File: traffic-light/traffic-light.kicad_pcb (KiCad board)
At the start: 2 copper layers, 11 parts, among them J1 Conn_01x04_Male

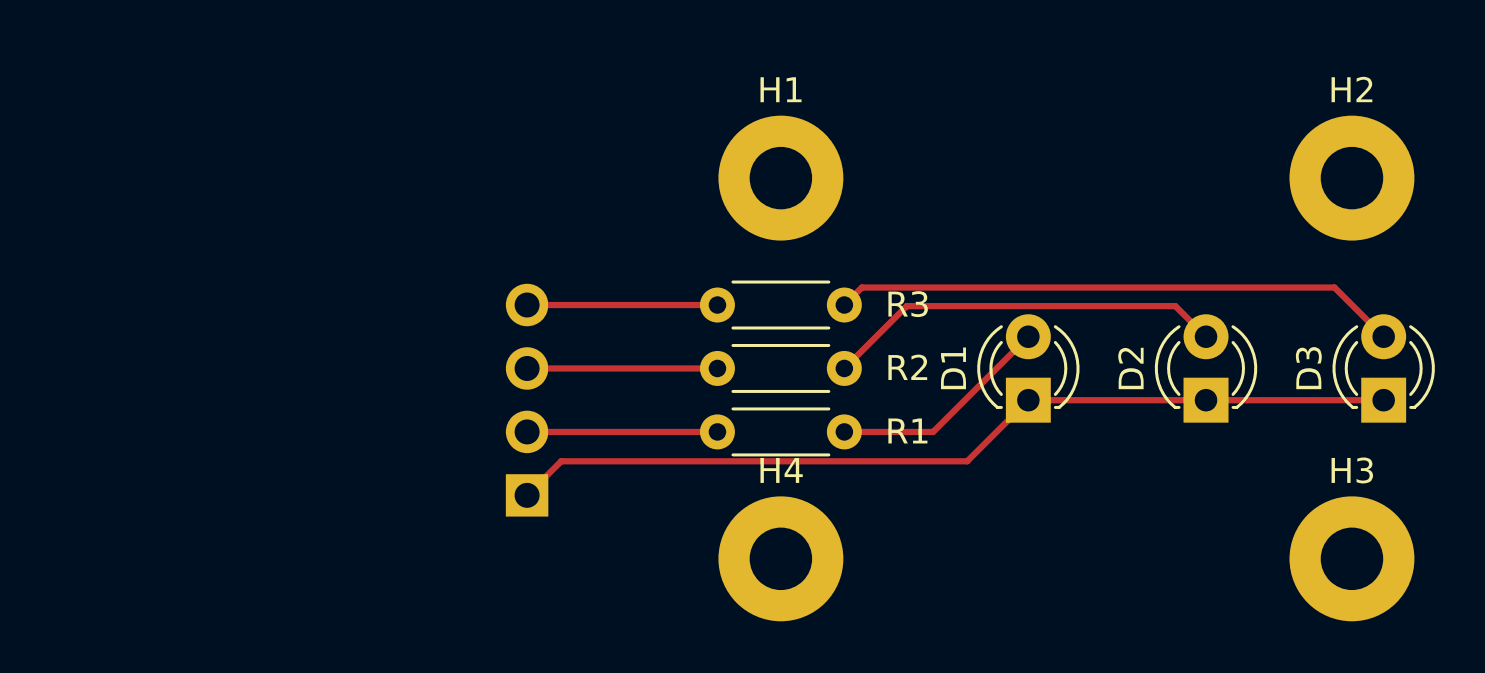
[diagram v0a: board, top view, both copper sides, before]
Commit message: traffic-light: add round edges, correct pin header, add silk screen
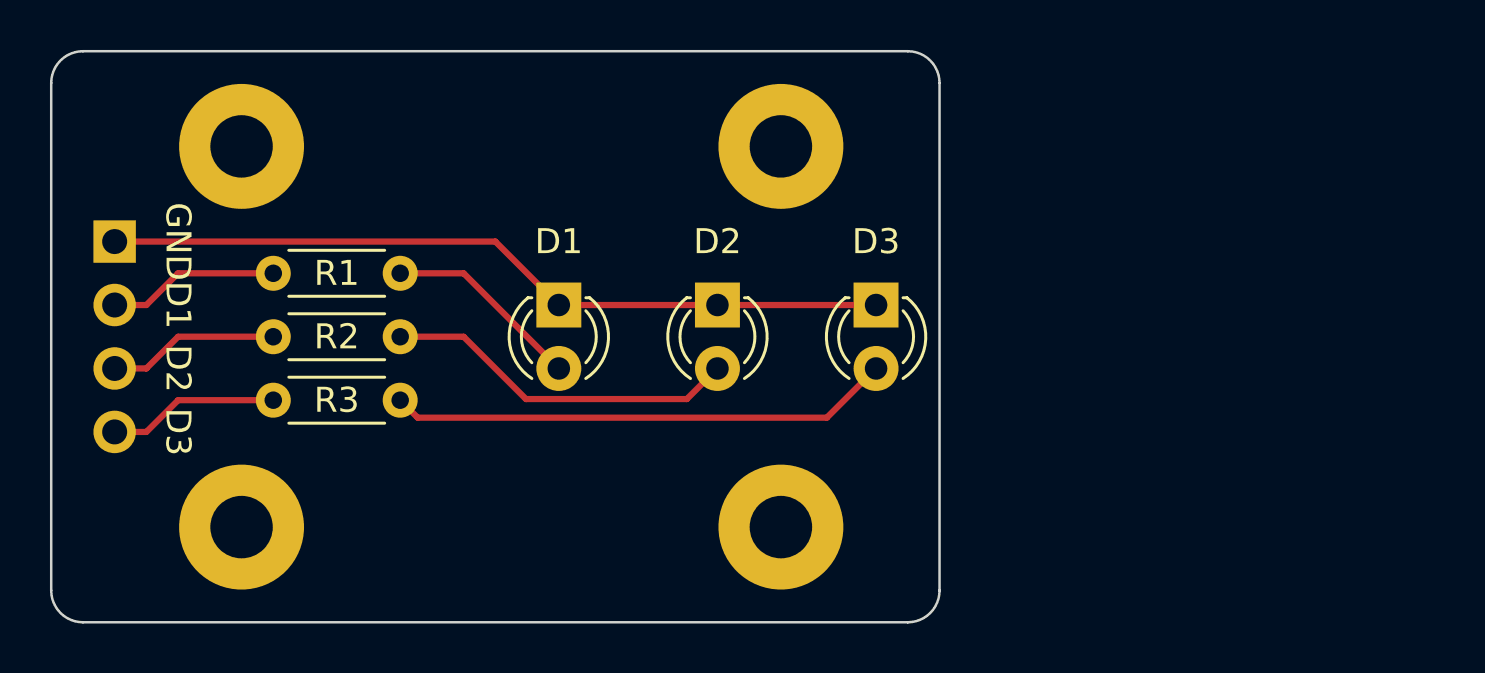
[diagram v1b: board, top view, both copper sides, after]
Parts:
- J1: value Conn_01x04_Male -> Conn_01x04_Female; footprint Connector_PinSocket_2.54mm:PinSocket_1x04_P2.54mm_Horizontal -> Connector_PinHeader_2.54mm:PinHeader_1x04_P2.54mm_Horizontal
- moved H3 44.5 mm to (118.1, 95.2)
- moved H2 22.9 mm to (139.7, 80.0)
- moved H1 21.6 mm to (118.1, 80.0)
- moved D3 20.7 mm to (143.5, 86.4), turned to 270 degrees
- moved D2 19.9 mm to (137.2, 86.4), turned to 270 degrees
- moved J1 19.4 mm to (113.0, 83.8), turned to 180 degrees
- moved D1 19.2 mm to (130.8, 86.4), turned to 270 degrees
- moved R1 18.9 mm to (124.5, 85.1)
- moved R3 18.2 mm to (124.5, 90.2)
- moved R2 17.8 mm to (124.5, 87.6)
- moved H4 1.27 mm to (139.7, 95.2)
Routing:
- net Net-(D1-Pad1): track 36.3 -> 31.5 mm
- net Net-(D3-Pad2): track 22.7 -> 20.2 mm
- net Net-(D2-Pad2): track 16.0 -> 14.2 mm
- net Net-(D1-Pad2): track 8.94 -> 7.93 mm
- net Net-(J1-Pad4): track 7.62 -> 6.88 mm
- net Net-(J1-Pad2): track 7.62 -> 6.88 mm
- net Net-(J1-Pad3): track 7.62 -> 6.88 mm
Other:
- board outline added: 35.6 x 22.9 mm
- board text added: "D1"
- board text added: "D2"
- board text added: "D3"
- board text added: "GND"

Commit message: traffic-light: decrease pcb size, add gerbers, pcb is ready to order
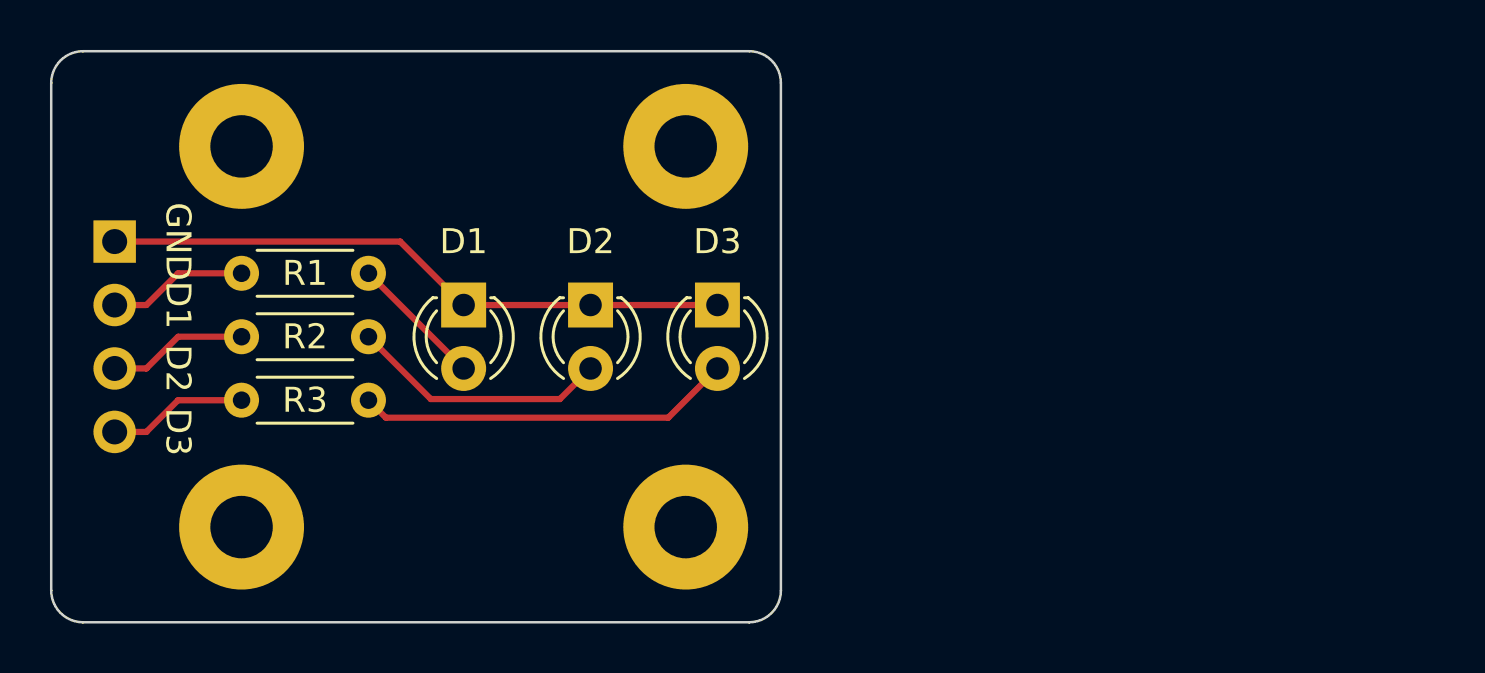
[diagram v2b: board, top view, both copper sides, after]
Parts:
- moved D3 6.35 mm to (137.2, 86.4)
- moved D2 5.08 mm to (132.1, 86.4)
- moved D1 3.81 mm to (127.0, 86.4)
- moved H2 3.81 mm to (135.9, 80.0)
- moved H4 3.81 mm to (135.9, 95.2)
- moved R1 1.27 mm to (123.2, 85.1)
- moved R2 1.27 mm to (123.2, 87.6)
- moved R3 1.27 mm to (123.2, 90.2)
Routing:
- net Net-(D1-Pad1): track 31.5 -> 25.2 mm
- net Net-(D3-Pad2): track 20.2 -> 15.1 mm
- net Net-(D2-Pad2): track 14.2 -> 10.4 mm
- net Net-(D1-Pad2): track 7.93 -> 5.39 mm
- net Net-(J1-Pad4): track 6.88 -> 5.61 mm
- net Net-(J1-Pad3): track 6.88 -> 5.61 mm
- net Net-(J1-Pad2): track 6.88 -> 5.61 mm
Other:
- board size 35.6 x 22.9 mm -> 29.2 x 22.9 mm

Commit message: traffic-light: update edge cuts
Signed-off-by: Sean Tedesco <stedesco@live.com>
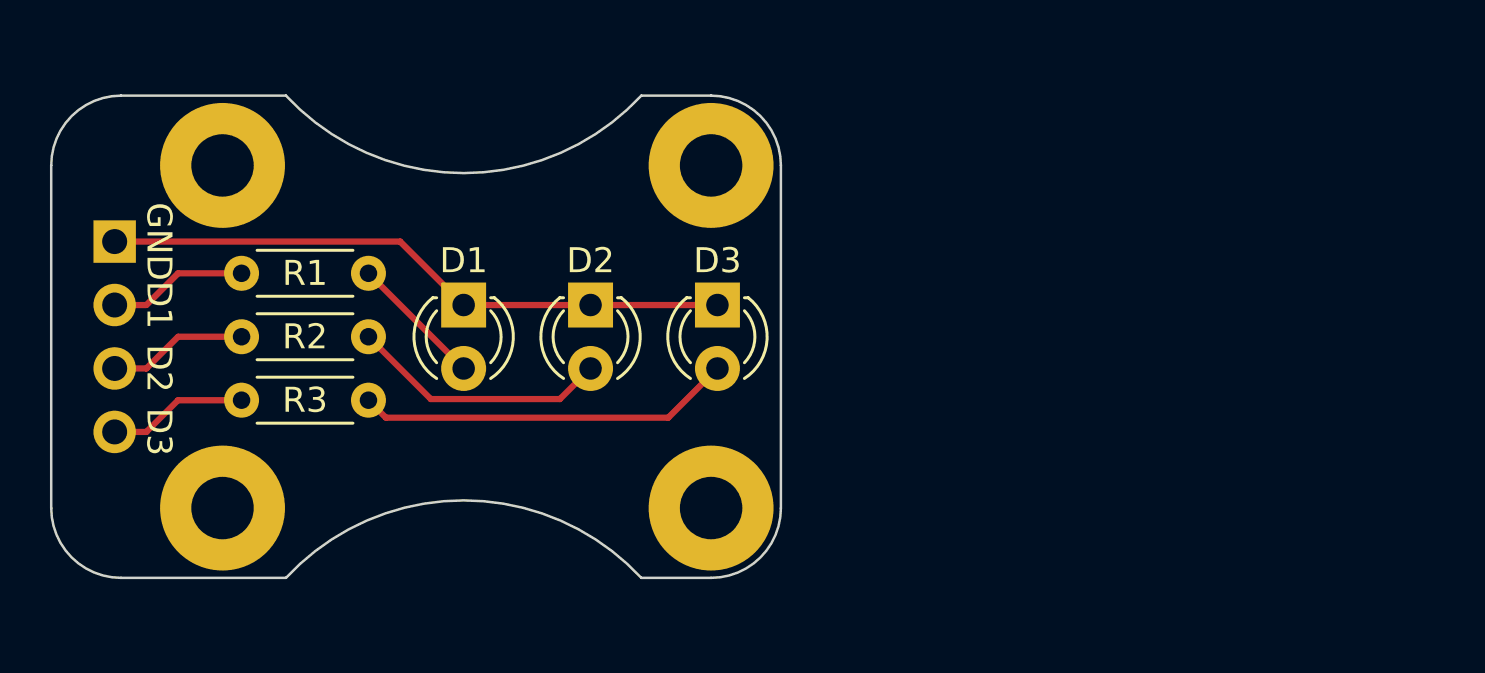
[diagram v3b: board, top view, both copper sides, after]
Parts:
- moved H2 1.27 mm to (136.9, 80.8)
- moved H4 1.27 mm to (136.9, 94.5)
- moved H1 1.08 mm to (117.3, 80.8)
- moved H3 1.08 mm to (117.3, 94.5)
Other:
- board size 29.2 x 22.9 mm -> 29.2 x 19.3 mm
